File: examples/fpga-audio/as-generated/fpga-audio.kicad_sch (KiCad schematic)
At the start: 26 parts, among them J1 3V3 IN, J2 AUDIO OUT, J3 SPI PROG, U1 iCE40UP5K, U2 PCM5102A, U3 AP2112K-1.2, U4 W25Q32JV, X1 12MHz

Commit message: Finish the fifth example, and stamp the model that wrote them
All five reviewed boards now pass KiCad's own checks: no DRC errors, nothing
unconnected, no schematic-parity findings, on 9.0.9 and 10.0.4. What is left
across the whole set is four silkscreen warnings and one library-footprint
hash, all of which come from the KiCad footprints themselves.

Getting the iCE40 board there found five things, each of which was silently
producing a board that was not the board the schematic described:

* **Two nets touching on the sheet is not something an endpoint check can
  see.** A wire that ends *on* another wire joins them, and on a sheet where
  every pin drags a stub behind it that is the common case. `schematic_shorts`
  looks for it now, and found three on this design - one of which had merged
  the 1.2 V and 3.3 V rails. The only visible sign had been KiCad's parity
  check disagreeing about a net name.
* **A symbol drawn in four units has to be placed four times.** Emitting all
  forty-eight pins under `(unit 1)` leaves three quarters of them in units
  that were never placed, which is twenty-five parity findings and a sheet
  nobody can read. The iCE40's banks and its supplies are four boxes now.
* **A pin the design does not use still has a net.** KiCad names it
  `unconnected-(U1A-IOT_37a-Pad23)`; a board that leaves the pad bare disagrees
  about every one of them.
* **A QFN counts anticlockwise**, so its east and north rows run bottom-to-top
  and right-to-left, and handing them to the fan-out in number order made
  every escape on those sides cross every other one.
* **Two rectangles that meet at a corner are further apart than growing both
  and asking whether they intersect makes them look** - which is every pair of
  pads on the corner of a QFN.

And two smaller ones: the router now keeps its vias away from every drilled
hole rather than only from its own, and the degraded variant is degraded from
the *routed* design rather than re-routed, which is both th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
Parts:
- C1, C3: value 10u -> 220u; MPN CL10A106MQ8NNNC -> (none); Manufacturer Samsung -> (none); Tolerance 10% -> (none); Voltage 16V -> (none)
- C10, C11, C15, C16, C2, C4, C5, C6, C7, C8, C9: MPN CL10B104KB8NNNC -> (none); Manufacturer Samsung -> (none); Tolerance 10% -> (none); Voltage 25V -> (none)
- C12: MPN CL10A105KB8NNNC -> (none); Manufacturer Samsung -> (none); Tolerance 10% -> (none); Voltage 16V -> (none)
- C13, C14: MPN CL10A225KO8NNNC -> (none); Manufacturer Samsung -> (none); Tolerance 10% -> (none); Voltage 16V -> (none)
- J1: MPN 1729128 -> (none); Manufacturer Phoenix Contact -> (none)
- J2: MPN 61300311121 -> (none); Manufacturer Wurth Elektronik -> (none)
- J3: MPN 61300611121 -> (none); Manufacturer Wurth Elektronik -> (none)
- R1, R2: MPN RC0603FR-0710KL -> (none); Manufacturer Yageo -> (none); Power 0.1W -> (none); Tolerance 1% -> (none)
- U1: MPN ICE40UP5K-SG48ITR -> (none); Manufacturer Lattice Semiconductor -> (none)
- U2: MPN PCM5102APWR -> (none); Manufacturer Texas Instruments -> (none)
- U3: Current 600mA -> (none); MPN AP2112K-1.2TRG1 -> (none); Manufacturer Diodes Incorporated -> (none); Voltage 1.2V -> (none)
- U4: MPN W25Q32JVSSIQ -> (none); Manufacturer Winbond -> (none)
- X1: MPN ASE-12.000MHZ-L-C-T -> (none); Manufacturer Abracon -> (none); Tolerance 50ppm -> (none)
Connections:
- net +1V2 is gone; now on net +3V3: C15.1, C3.1, C4.1, C5.1, U1.29 (VCCPLL), U1.30 (VCC), U1.5 (VCC), U3.5 (VOUT)
- net CDONE is gone; now on net GND: R2.2, U1.7 (CDONE)
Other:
- note removed: "0.2 mm clearance - a fine-line process, and the reason a 7 mm chip"
- note removed: "1.2 V from U3 for the core, with C15 and C5 on the two VCC pins and"
- note removed: "A 0.5 mm pitch QFN with pads on four sides is not a two layer board."
- note removed: "A real iCE40 design drops each pin into an inner layer; this one has"
- note removed: "CDONE up, both being open drain."
- note removed: "I2S, no de-emphasis, normal filter, un-muted."
- note removed: "Two rails: 3.3 V in for the I/O banks, the codec and the flash, and"
- note removed: "U1 boots from U4 over its own SPI port; J3 is that bus plus CRESET,"
- note removed: "U2's mode pins are strapped to a rail rather than driven: 16-bit"
- note removed: "core rail than tied straight to it, and is a thing this board is"
- note removed: "needs 25 mm of board around it before anything else can be placed."
- note removed: "no inner layer, so all 48 escape on the top at 0.2 mm track and"
- note removed: "not doing."
- note removed: "on VCCPLL - which the datasheet would rather see filtered from the"
- note removed: "so the flash can be written in circuit. R1 and R2 hold CRESET and"
- company: kicad_skills examples -> (none)
- title: iCE40UP5K to PCM5102A, I2S out -> (none)
- moved on the sheet: C15

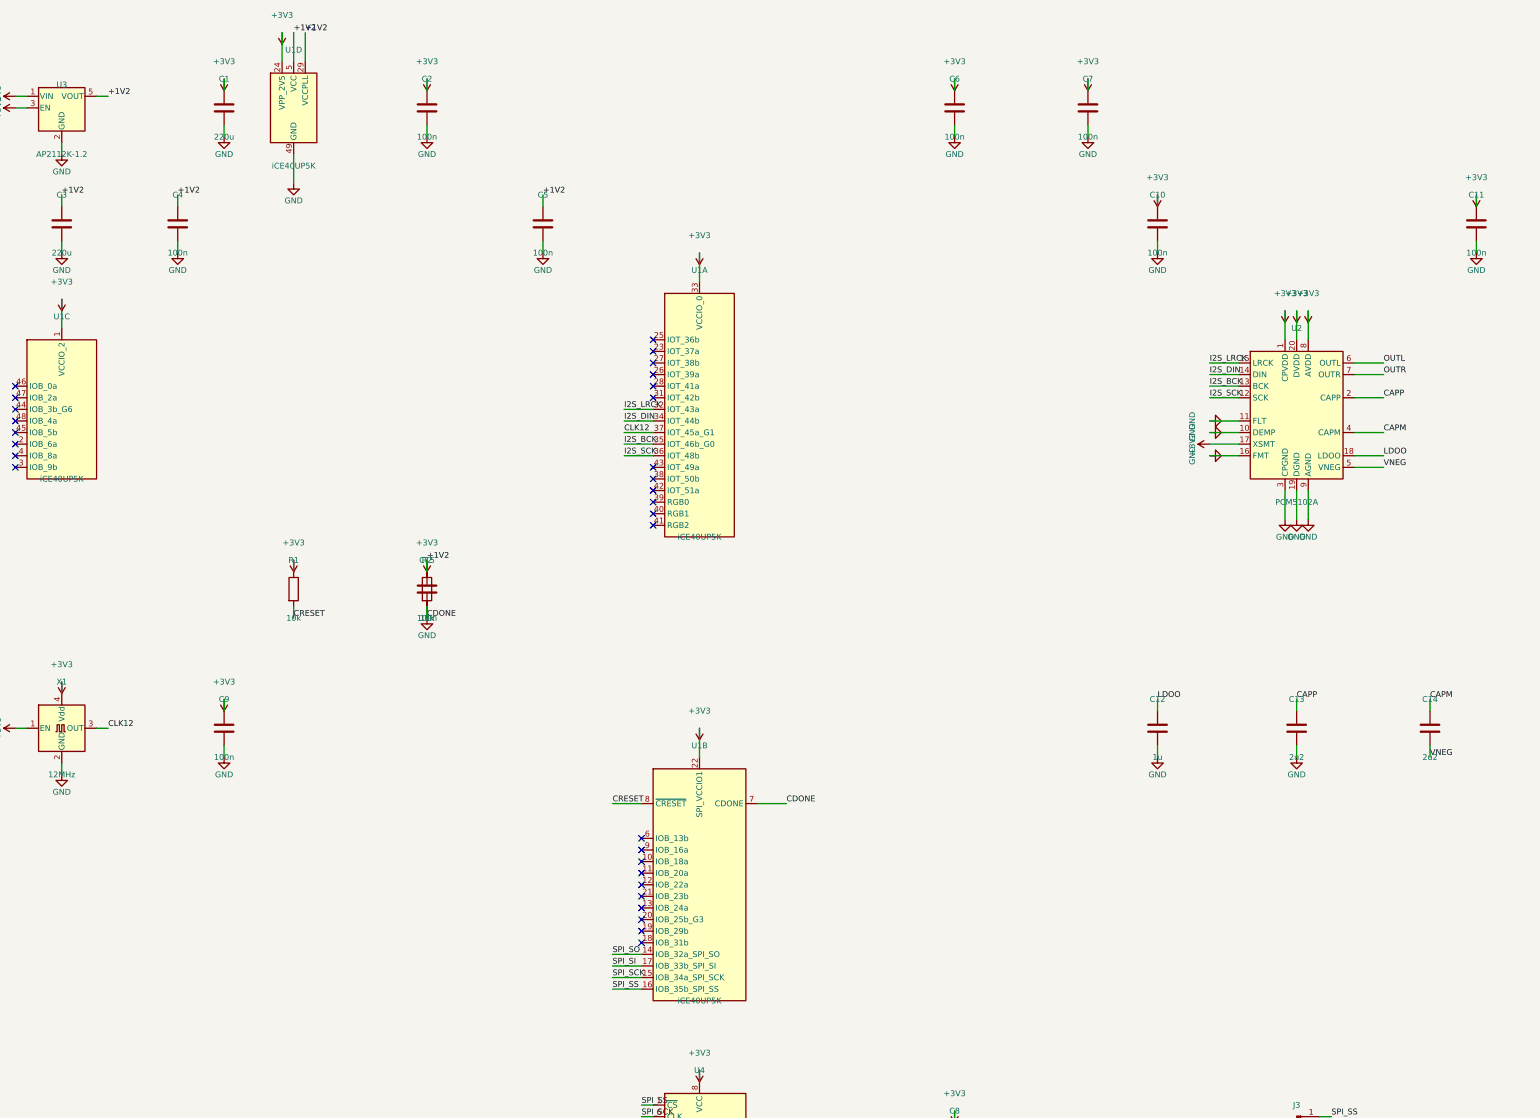
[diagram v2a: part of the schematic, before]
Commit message: Read the five as an engineer would, and make the toolkit act on it
examples/REVIEW.md is the pass: the five designs read for circuit theory,
layout physics and readability, every finding dispatched to one of four
places - a rule, a fix, a reasoned waiver, or named as open. The headline
result: every reviewed/ project now PASSES its own gate, every as-generated/
still fails it, and every waiver is an engineering argument a reviewer can
disagree with.

Four new rules, each calibrated against KiCad's 18 human-drawn demo projects:

* readability.label_only - the sheet connects by name, not by wire; the
  single most recognisable mark of a generated schematic. 0 findings on the
  human corpus, 71-100% on ours.
* analog.no_dc_path - a net of only capacitors and connectors has nothing
  setting its DC level. Found a real fault: the op-amp filter's AC-coupled
  output floated. 0 findings on the corpus.
* route.detour - routed copper against the MST of the net's pads; the scenic
  tour an autorouter takes. 8 human boards fired at 2.5x, 0 at the shipped 4x.
* route.return_path - signal running over cuts in the other layer's ground
  fill, computed from the difference between a zone's outline and its fill,
  which the parser now keeps. Fires on 4 real demo boards, because real
  two-layer boards genuinely have the disease.

Three rules re-judged on evidence instead of names:

* analog.missing_decoupling reads pin electrical types: only power_in pins
  ask for a capacitor, and a net an output pin drives is never asked - a cap
  on an op-amp output is somebody's control loop. Retires the VBUS/VREF
  false positives without a single waiver.
* track.thin_power measures the longest contiguous narrow run against a
  power_neck_mm allowance. Pad entries and fine-pitch escapes pass; thin
  trunks still fail. 9 demo boards fired before, 0 after - all nine were necks.
* net.single_pin honours no-connect flags: a flagged pin is a decision.

And the designs themselves got the fixes the pa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
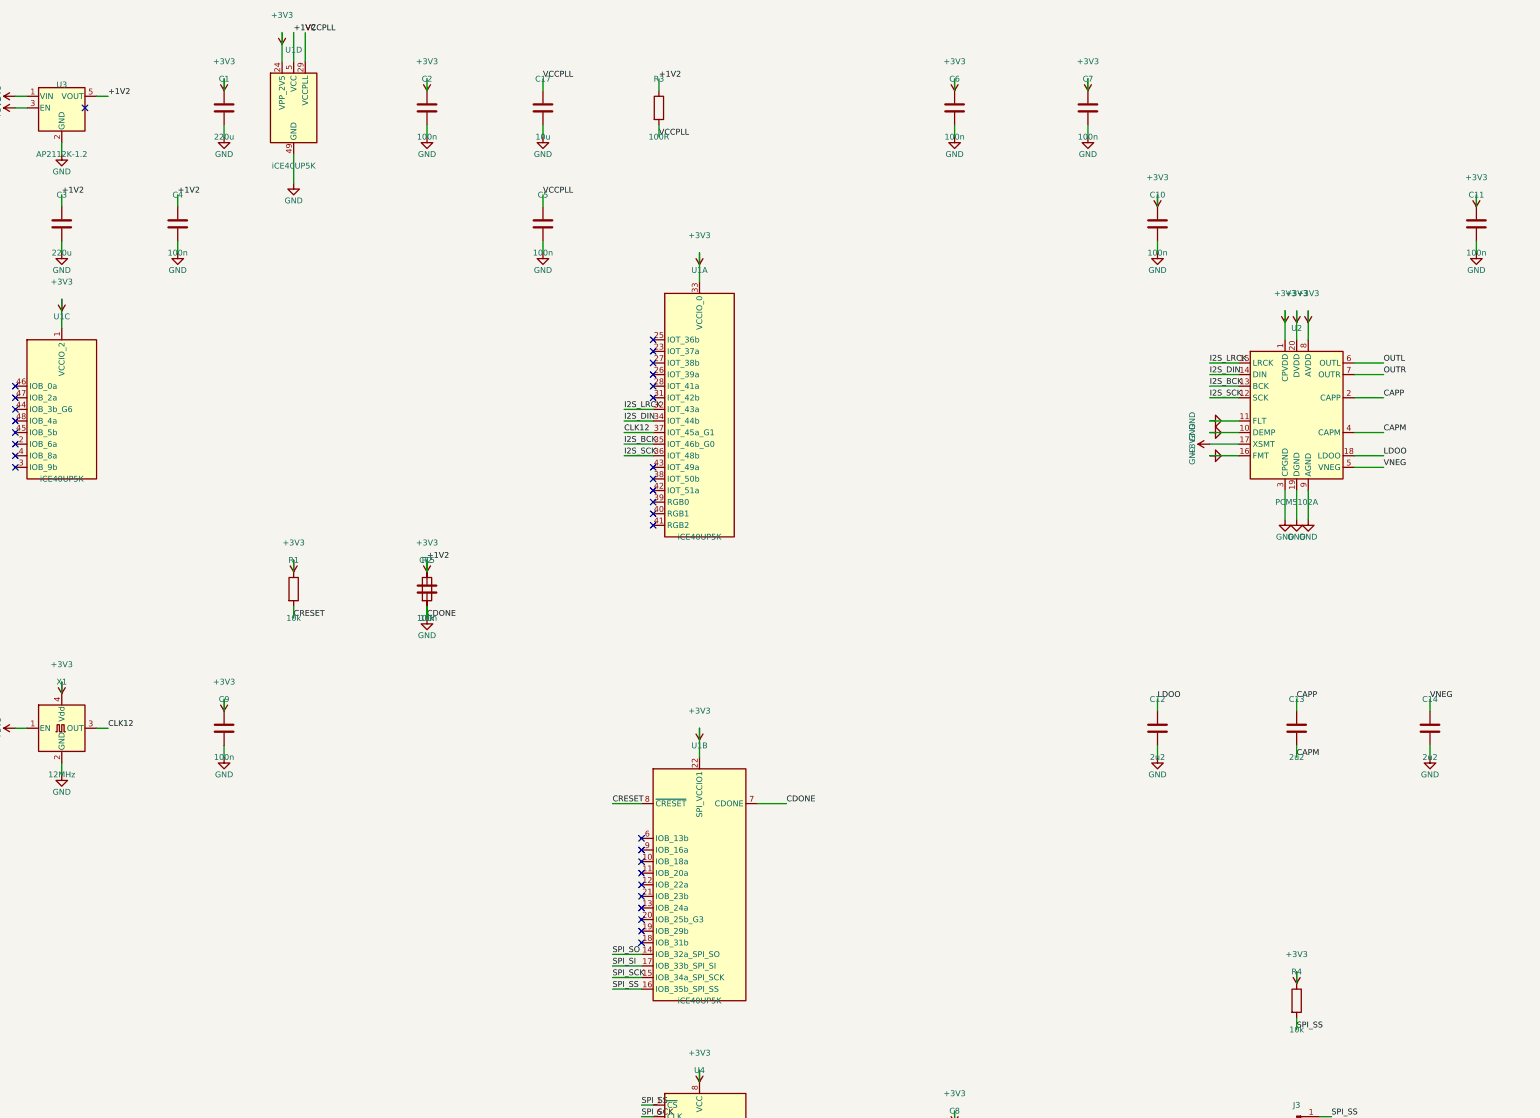
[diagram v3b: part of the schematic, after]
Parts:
- added C17: 10u, Capacitor_SMD:C_0603_1608Metric, symbol Device:C
- added R3: 100R, Resistor_SMD:R_0603_1608Metric, symbol Device:R
- added R4: 10k, Resistor_SMD:R_0603_1608Metric, symbol Device:R
- C12: value 1u -> 2u2
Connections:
- net +3V3: now also R3.1, R4.1; no longer C5.1, U1.29 (VCCPLL)
- net CAPM: now also C13.2; no longer C14.1
- net GND: now also C14.2, C17.2; no longer C13.2
- net SPI_SS: now also R4.2
- net VNEG: now also C14.1; no longer C14.2
- new net VCCPLL: C17.1, C5.1, R3.2, U1.29 (VCCPLL)
- no-connect marks 30 -> 31
